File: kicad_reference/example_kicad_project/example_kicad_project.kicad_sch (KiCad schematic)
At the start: 3 parts, among them U1 NCP1117-3.3_SOT223

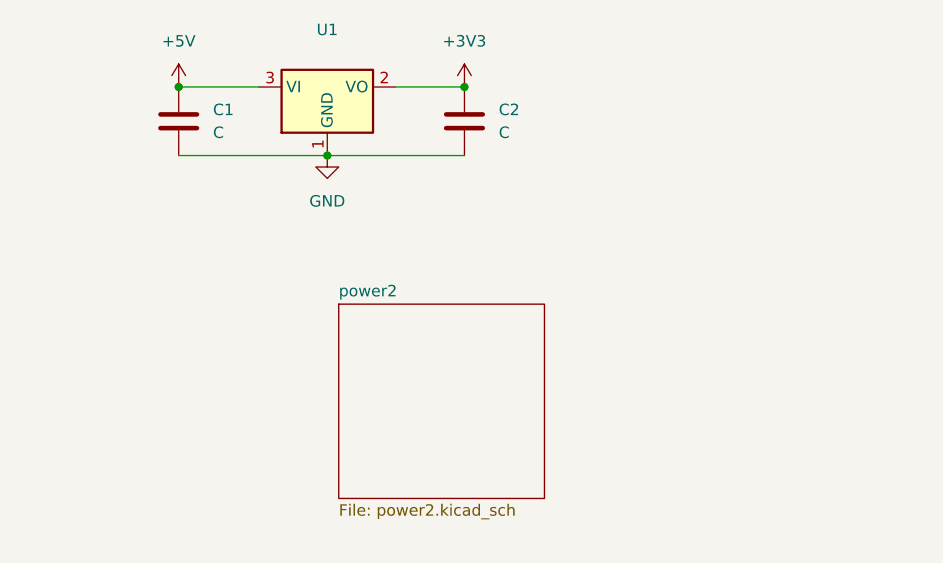
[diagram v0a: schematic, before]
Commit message: modified example to be hierarchical. add kicad_to_skidl script
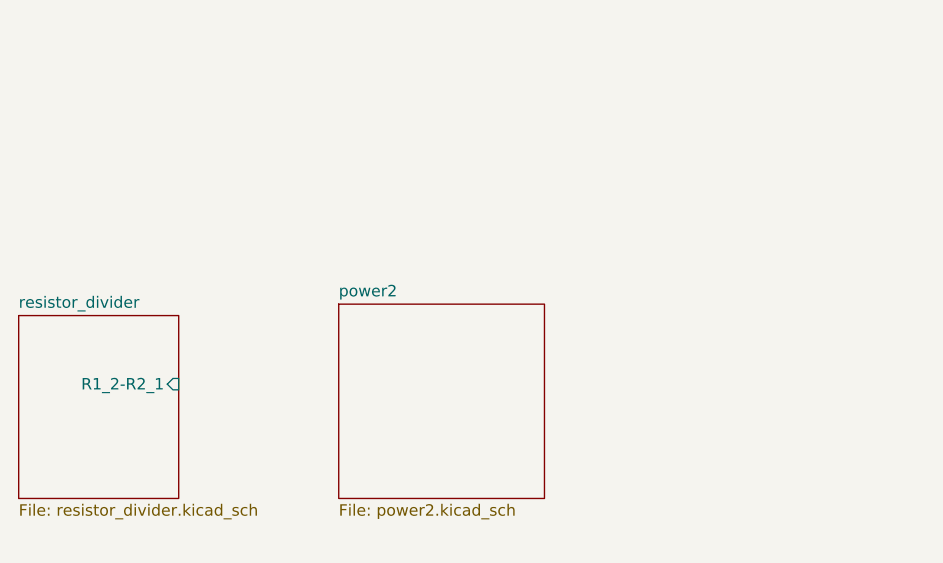
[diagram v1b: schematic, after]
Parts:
- removed C1, C2: C, Capacitor_SMD:C_0603_1608Metric, symbol Device:C
- removed U1: NCP1117-3.3_SOT223, Package_TO_SOT_SMD:SOT-223-3_TabPin2, symbol Regulator_Linear:NCP1117-3.3_SOT223
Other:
- added sheet resistor_divider (resistor_divider.kicad_sch)

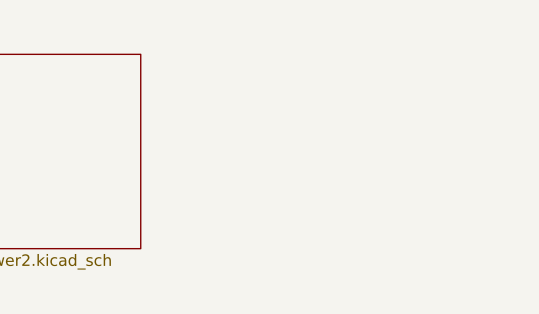
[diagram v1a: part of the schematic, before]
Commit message: updating logic to handle more circuits
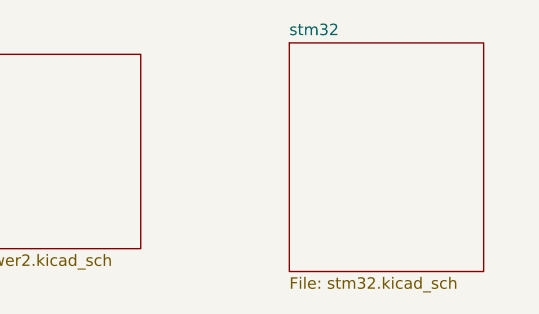
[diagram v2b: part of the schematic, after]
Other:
- added sheet stm32 (stm32.kicad_sch)
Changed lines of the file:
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@@
+		)
+	)
+	(sheet
+		(at 111.76 45.72)
+		(size 21.59 25.4)
+		(fields_autoplaced yes)
+		(stroke
+			(width 0.1524)
+			(type solid)
+		)
+		(fill
+			(color 0 0 0 0.0000)
+		)
+		(property "Sheetname" "stm32"
+			(at 111.76 45.0084 0)
+			(effects
+				(font
+					(size 1.27 1.27)
+				)
+				(justify left bottom)
+			)
+		)
+		(property "Sheetfile" "stm32.kicad_sch"
+			(at 111.76 71.7046 0)
+			(effects
+				(font
+					(size 1.27 1.27)
+				)
+				(justify left top)
+			)
+		)
+		(instances
+			(project "example_kicad_project"
+				(path "/139408cf-b4ac-4ccf-8751-afbb6def1f13"
+					(page "4")
+				)
+			)
 		)
 	)
